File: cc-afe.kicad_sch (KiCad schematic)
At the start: 10 parts

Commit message: Finish Regulator section
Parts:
- renumbered MT5 to MT4, MT7 to MT5, MT8 to MT6
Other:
- sheet zuDFE Connectors ports: added SFP0{TRX}, SFP1{TRX}, SFP2{TRX}, SFP3{TRX}, SFP4{TRX}, SFP5{TRX}, SFP6{TRX}, SFP7{TRX}; removed none
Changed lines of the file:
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@@
+		)
+	)
+	(bus
+		(pts
+			(xy 214.63 119.38) (xy 241.3 119.38)
+		)
+		(stroke
+			(width 0)
+			(type default)
+		)
+	)
+	(bus
+		(pts
+			(xy 214.63 106.68) (xy 241.3 106.68)
+		)
+		(stroke
+			(width 0)
+			(type default)
 		)
 	)
@@
 		)
 	)
+	(bus
+		(pts
+			(xy 214.63 104.14) (xy 241.3 104.14)
+		)
+		(stroke
+			(width 0)
+			(type default)
+		)
+	)
 	(wire
 		(pts
@@
 		)
 	)
+	(bus
+		(pts
+			(xy 214.63 116.84) (xy 241.3 116.84)
+		)
+		(stroke
+			(width 0)
+			(type default)
+		)
+	)
 	(wire
 		(pts
@@
 		)
 	)
+	(bus
+		(pts
+			(xy 214.63 101.6) (xy 241.3 101.6)
+		)
+		(stroke
+			(width 0)
+			(type default)
+		)
+	)
 	(wire
 		(pts
 			(xy 344.17 208.28) (xy 344.17 207.01)
+		)
+		(stroke
+			(width 0)
+			(type default)
+		)
+	)
+	(bus
+		(pts
+			(xy 214.63 111.76) (xy 241.3 111.76)
+		)
+		(stroke
+			(width 0)
+			(type default)
+		)
+	)
+	(bus
+		(pts
+			(xy 214.63 109.22) (xy 241.3 109.22)
+		)
+		(stroke
+			(width 0)
+			(type default)
+		)
+	)
+	(bus
+		(pts
+			(xy 214.63 114.3) (xy 241.3 114.3)
 		)
 		(stroke
@@
 		(dnp no)
 		(fields_autoplaced yes)
-		(property "Reference" "#PWR013"
+		(property "Reference" "#PWR010"
 			(at 386.08 194.31 0)
 			(effects
@@
 			(project "cc-afe"
 				(path "/40891cc8-bf64-41f4-8f69-a607d7b280eb"
-					(reference "#PWR013")
+					(reference "#PWR010")
 					(unit 1)
 				)
@@
 		(dnp no)
 		(fields_autoplaced yes)
-		(property "Reference" "MT8"
+		(property "Reference" "MT6"
 			(at 388.62 181.6099 0)
 			(effects
@@
 			(project "cc-afe"
 				(path "/40891cc8-bf64-41f4-8f69-a607d7b280eb"
-					(reference "MT8")
+					(reference "MT6")
 					(unit 1)
 				)
@@
 		(dnp no)
 		(fields_autoplaced yes)
-		(property "Reference" "MT5"
+		(property "Reference" "MT4"
 			(at 358.14 181.6099 0)
 			(effects
@@
 			(project "cc-afe"
 				(path "/40891cc8-bf64-41f4-8f69-a607d7b280eb"
-					(reference "MT5")
+					(reference "MT4")
 					(unit 1)
 				)
@@
 		(dnp no)
 		(fields_autoplaced yes)
-		(property "Reference" "#PWR08"
+		(property "Reference" "#PWR07"
 			(at 355.6 194.31 0)
 			(effects
@@
 			(project "cc-afe"
 				(path "/40891cc8-bf64-41f4-8f69-a607d7b280eb"
-					(reference "#PWR08")
+					(reference "#PWR07")
 					(unit 1)
 				)
@@
 		(dnp no)
 		(fields_autoplaced yes)
-		(property "Reference" "#PWR09"
+		(property "Reference" "#PWR08"
 			(at 359.41 214.63 0)
 			(effects
@@
 			(project "cc-afe"
 				(path "/40891cc8-bf64-41f4-8f69-a607d7b280eb"
-					(reference "#PWR09")
+					(reference "#PWR08")
 					(unit 1)
 				)
@@
 		(dnp no)
 		(fields_autoplaced yes)
-		(property "Reference" "#PWR012"
+		(property "Reference" "#PWR09"
 			(at 375.92 194.31 0)
 			(effects
@@
 			(project "cc-afe"
 				(path "/40891cc8-bf64-41f4-8f69-a607d7b280eb"
-					(reference "#PWR012")
+					(reference "#PWR09")
 					(unit 1)
 				)
@@
 		(dnp no)
 		(fields_autoplaced yes)
-		(property "Reference" "MT7"
+		(property "Reference" "MT5"
 			(at 378.46 181.6099 0)
 			(effects
@@
 			(project "cc-afe"
 				(path "/40891cc8-bf64-41f4-8f69-a607d7b280eb"
-					(reference "MT7")
+					(reference "MT5")
 					(unit 1)
 				)
@@
 	)
 	(sheet
-		(at 240.665 99.06)
-		(size 29.845 43.18)
+		(at 241.3 99.06)
+		(size 29.21 43.18)
 		(exclude_from_sim no)
 		(in_bom yes)
@@
 		)
 		(property "Sheetname" "SFP"
-			(at 240.665 98.3484 0)
+			(at 241.3 98.3484 0)
 			(effects
 				(font
@@
 		)
 		(property "Sheetfile" "sfp.kicad_sch"
-			(at 240.665 142.8246 0)
+			(at 241.3 142.8246 0)
 			(effects
 				(font
@@
 		)
 		(pin "SFP2{TRX}" bidirectional
-			(at 240.665 106.68 180)
+			(at 241.3 106.68 180)
 			(effects
 				(font
@@
 		)
 		(pin "SFP1{TRX}" bidirectional
-			(at 240.665 104.14 180)
+			(at 241.3 104.14 180)
 			(effects
 				(font
@@
 		)
 		(pin "SFP0{TRX}" bidirectional
-			(at 240.665 101.6 180)
+			(at 241.3 101.6 180)
 			(effects
 				(font
@@
 		)
 		(pin "SFP3{TRX}" bidirectional
-			(at 240.665 109.22 180)
+			(at 241.3 109.22 180)
 			(effects
 				(font
@@
 		)
 		(pin "I2C0{SDA,SCL}" bidirectional
-			(at 240.665 138.43 180)
+			(at 241.3 138.43 180)
 			(effects
 				(font
@@
 		)
 		(pin "SFP4{TRX}" bidirectional
-			(at 240.665 111.76 180)
+			(at 241.3 111.76 180)
 			(effects
 				(font
@@
 		)
 		(pin "SFP7{TRX}" bidirectional
-			(at 240.665 119.38 180)
+			(at 241.3 119.38 180)
 			(effects
 				(font
@@
 		)
 		(pin "SFP_MOD_ABS[7..0]" output
-			(at 240.665 130.81 180)
+			(at 241.3 130.81 180)
 			(effects
 				(font
@@
 		)
 		(pin "SFP_TX_DIS[7..0]" input
-			(at 240.665 128.27 180)
+			(at 241.3 128.27 180)
 			(effects
 				(font
@@
 		)
 		(pin "SFP_RX_LOS[7..0]" output
-			(at 240.665 125.73 180)
+			(at 241.3 125.73 180)
 			(effects
 				(font
@@
 		)
 		(pin "SFP5{TRX}" bidirectional
-			(at 240.665 114.3 180)
+			(at 241.3 114.3 180)
 			(effects
 				(font
@@
 		)
 		(pin "SFP6{TRX}" bidirectional
-			(at 240.665 116.84 180)
+			(at 241.3 116.84 180)
 			(effects
 				(font
@@
 			(effects
 				(font
+					(size 1.27 1.27)
+				)
+				(justify right)
+			)
+		)
+		(pin "SFP4{TRX}" bidirectional
+			(at 214.63 111.76 0)
+			(effects
+				(font
+					(size 1.27 1.27)
+				)
+				(justify right)
+			)
+		)
+		(pin "SFP5{TRX}" bidirectional
+			(at 214.63 114.3 0)
+			(effects
+				(font
+					(size 1.27 1.27)
+				)
+				(justify right)
+			)
+		)
+		(pin "SFP6{TRX}" bidirectional
+			(at 214.63 116.84 0)
+			(effects
+				(font
+					(size 1.27 1.27)
+				)
+				(justify right)
+			)
+		)
+		(pin "SFP7{TRX}" bidirectional
+			(at 214.63 119.38 0)
+			(effects
+				(font
+					(size 1.27 1.27)
+				)
+				(justify right)
+			)
+		)
+		(pin "SFP0{TRX}" bidirectional
+			(at 214.63 101.6 0)
+			(effects
+				(font
+					(size 1.27 1.27)
+				)
+				(justify right)
+			)
+		)
+		(pin "SFP1{TRX}" bidirectional
+			(at 214.63 104.14 0)
+			(effects
+				(font
+					(size 1.27 1.27)
+				)
+				(justify right)
+			)
+		)
+		(pin "SFP2{TRX}" bidirectional
+			(at 214.63 106.68 0)
+			(effects
+				(font
+					(size 1.27 1.27)
+				)
+				(justify right)
+			)
+		)
+		(pin "SFP3{TRX}" bidirectional
+			(at 214.63 109.22 0)
+			(effects
+				(font

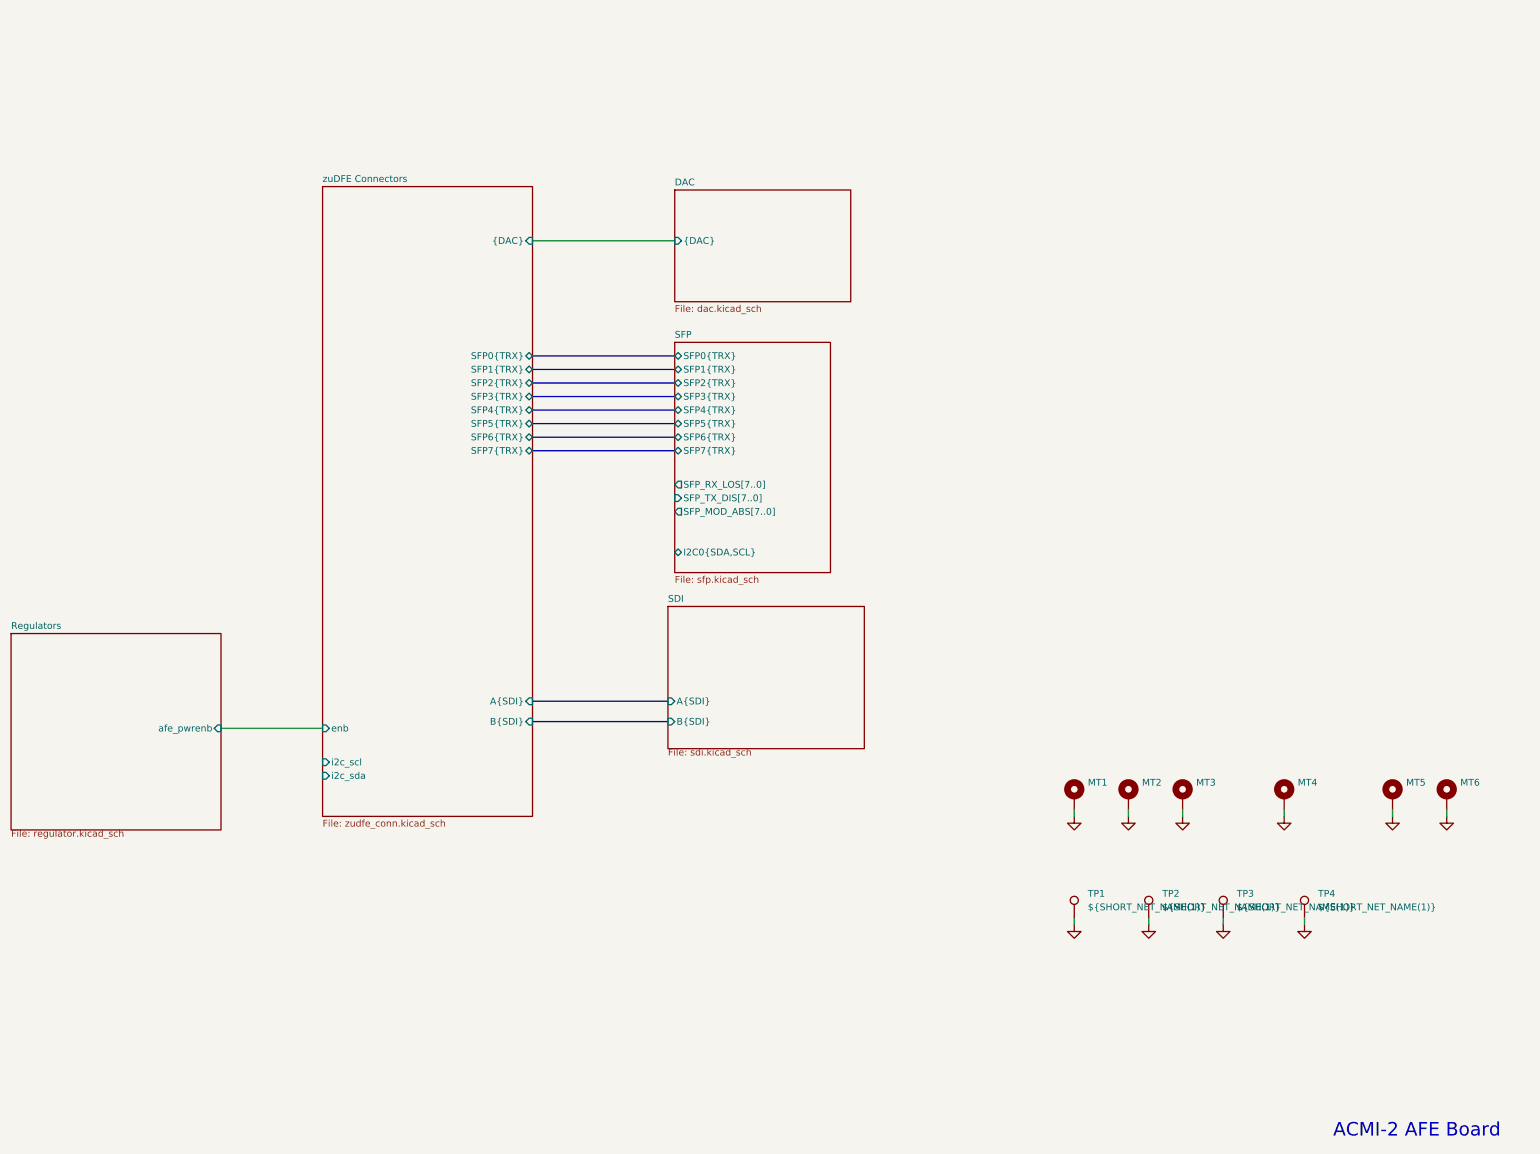
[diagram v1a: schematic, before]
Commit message: Place SFP passives
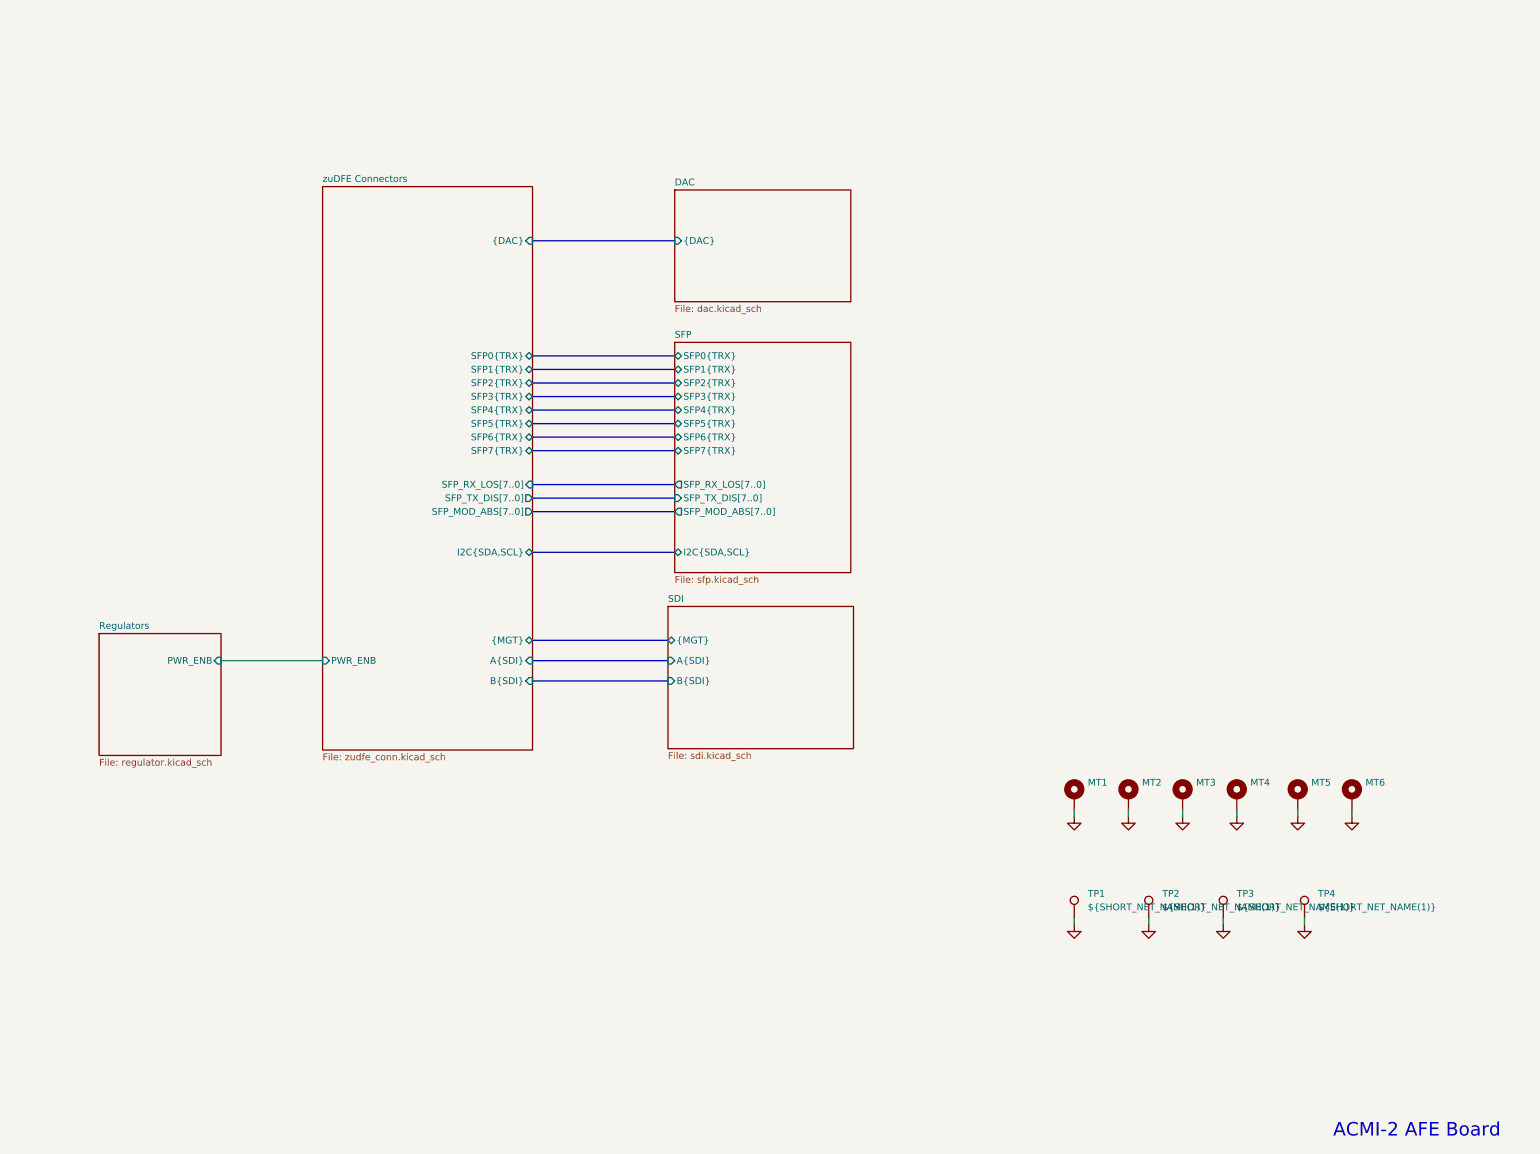
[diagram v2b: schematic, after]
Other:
- sheet Regulators ports: added PWR_ENB; removed afe_pwrenb
- sheet SDI ports: added {MGT}; removed none
- sheet SFP ports: added I2C{SDA,SCL}; removed I2C0{SDA,SCL}
- sheet zuDFE Connectors ports: added I2C{SDA,SCL}, PWR_ENB, SFP_MOD_ABS[7..0], SFP_RX_LOS[7..0], SFP_TX_DIS[7..0], {MGT}; removed enb, i2c_scl, i2c_sda
- moved on the sheet: MT4, MT5, MT6
